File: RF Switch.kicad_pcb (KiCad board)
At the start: 2 copper layers, 60 x 52 mm, 16 parts

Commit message: Add files via upload
added decoupling capacitors C1 and C2, repositioned R1, R2 and R3
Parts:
- added C1: C_Small, Capacitor_THT:CP_Radial_D5.0mm_P2.00mm, F.Cu at (103.2, 119.9)
- added C2: C_Small, Capacitor_THT:C_Disc_D5.0mm_W2.5mm_P2.50mm, F.Cu at (117.7, 117.9)
- J4: renamed from  
- moved R1 17.8 mm to (114.0, 144.1), turned to 180 degrees
- moved R2 6.80 mm to (139.1, 135.9), turned to 180 degrees
- moved R3 5.48 mm to (135.3, 139.2), turned to 180 degrees
- renumbered LED to D1, Power to J1, Switch to J2, Selector to SW2, ATTiny84 to U1
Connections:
- R1 pad 1: Net-(J4-Pad2) -> Net-(D1-Pad1)
- R1 pad 2: Net-(D1-Pad4) -> Net-(R1-Pad2)
- R2 pad 1: Net-(J4-Pad4) -> Net-(D1-Pad4)
- R2 pad 2: Net-(D1-Pad3) -> Net-(J4-Pad6)
- R3 pad 1: Net-(J2-Pad2) -> Net-(D1-Pad3)
- R3 pad 2: Net-(D1-Pad1) -> Net-(J4-Pad4)
- U1 pad 6: Net-(U1-Pad6) -> Net-(R1-Pad2)
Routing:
- net Net-(J4-Pad6): track 30.3 -> 60.8 mm
- net Net-(D1-Pad1): track 25.5 -> 4.30 mm
- net Net-(J4-Pad2): track 53.9 -> 33.7 mm
- net Net-(D1-Pad4): track 3.78 -> 19.8 mm
- net Net-(J2-Pad2): track 27.7 -> 17.4 mm
- net Net-(J4-Pad4): track 57.3 -> 47.0 mm
- net Net-(R1-Pad2): track 0.00 -> 10.2 mm
- net Net-(D1-Pad3): track 12.9 -> 19.6 mm
- net Net-(C2-Pad1): track 34.2 -> 35.3 mm
- net Net-(J4-Pad5): track 22.8 -> 23.8 mm
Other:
- board text added: "Designed by Electrifying Rides electrifyingrides.com.au"
- board text added: "JLCJLCJLCJLC"
- board text added: "RF Transmitter Button HW Ver 1 .0 - FW Ver 1.0"

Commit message: Add files via upload
Added pull up resistor and C1/C2
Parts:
- added 10k: 10k, Resistor_THT:R_Axial_DIN0207_L6.3mm_D2.5mm_P10.16mm_Horizontal, F.Cu at (136.6, 132.8)
-  : renamed from J4; value Conn_01x06 -> Programming Connector
- 100nF: renamed from C1; value C_Small -> 100nf ceramic; footprint Capacitor_THT:CP_Radial_D5.0mm_P2.00mm -> Capacitor_THT:C_Disc_D5.0mm_W2.5mm_P2.50mm
- 10uF: renamed from C2; value C_Small -> 10uF electrolytic; footprint Capacitor_THT:C_Disc_D5.0mm_W2.5mm_P2.50mm -> Capacitor_THT:CP_Radial_D5.0mm_P2.00mm
- J6: renamed from  ; value Conn_01x01 -> On/Off Switch
- OFF: value Conn_01x01 -> NC On/Off switch
- ON: value Conn_01x01 -> On/Off Switch
- RF Module: value Conn_01x04 -> RF Module Header
- moved 10uF 0.50 mm to (117.7, 118.4)
- renumbered R3 to 220, R2 to 220, R1 to 220, U1 to ATTiny84, J1 to Power, SW2 to Selector, J2 to Switch
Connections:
-   pad 1: GND -> +VDC
-   pad 3: +VDC -> Net-(J4-Pad3)
-   pad 6: Net-(J4-Pad6) -> GND
- 220 pad 2: Net-(J4-Pad6) -> Net-(J4-Pad5)
- ATTiny84 pad 4: Net-(J4-Pad5) -> Net-(J4-Pad3)
- ATTiny84 pad 7: Net-(J4-Pad6) -> Net-(J4-Pad5)
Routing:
- net Net-(J4-Pad6): track 60.8 -> 0.00 mm
- net Net-(J4-Pad5): track 23.8 -> 70.9 mm
- net Net-(J4-Pad3): track 0.00 -> 37.0 mm, vias 0 -> 1
- net Net-(J2-Pad2): track 17.4 -> 29.7 mm
- net Net-(U1-Pad5): track 0.00 -> 5.07 mm, vias 0 -> 1

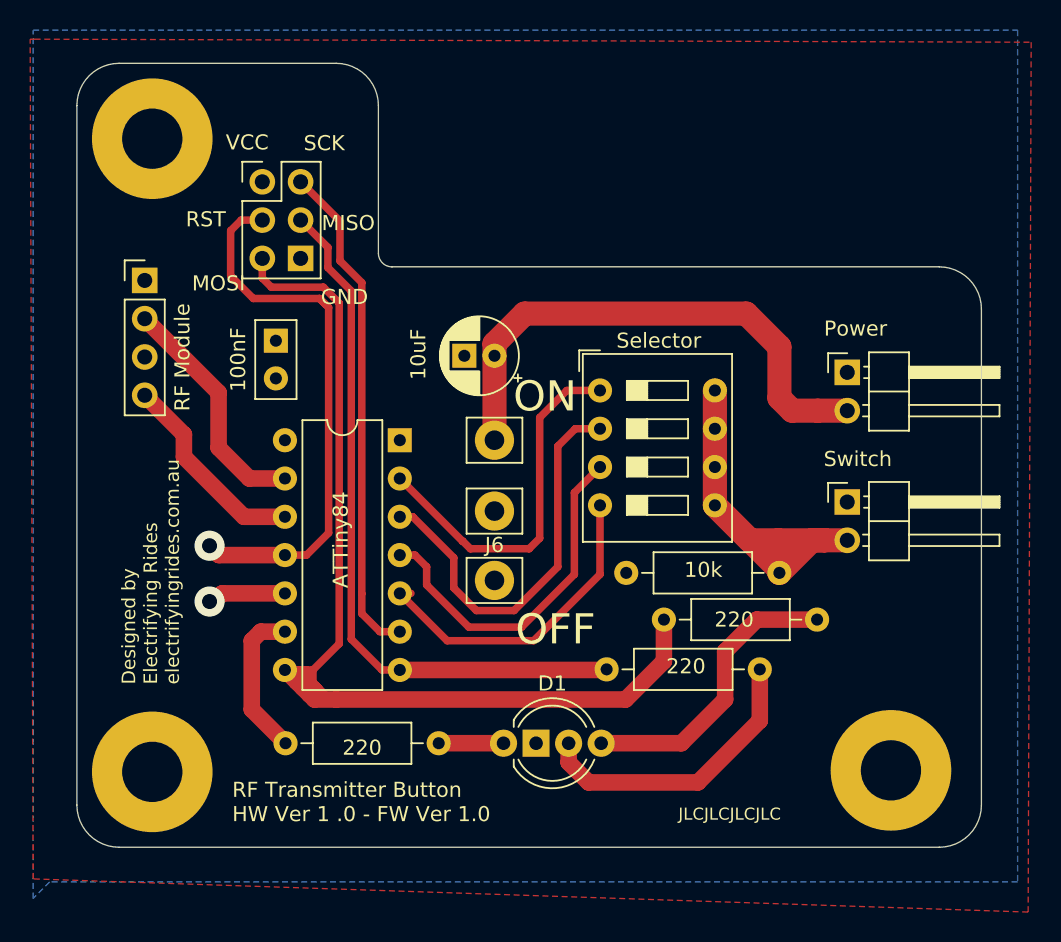
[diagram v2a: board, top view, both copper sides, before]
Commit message: Add files via upload
componet reposition
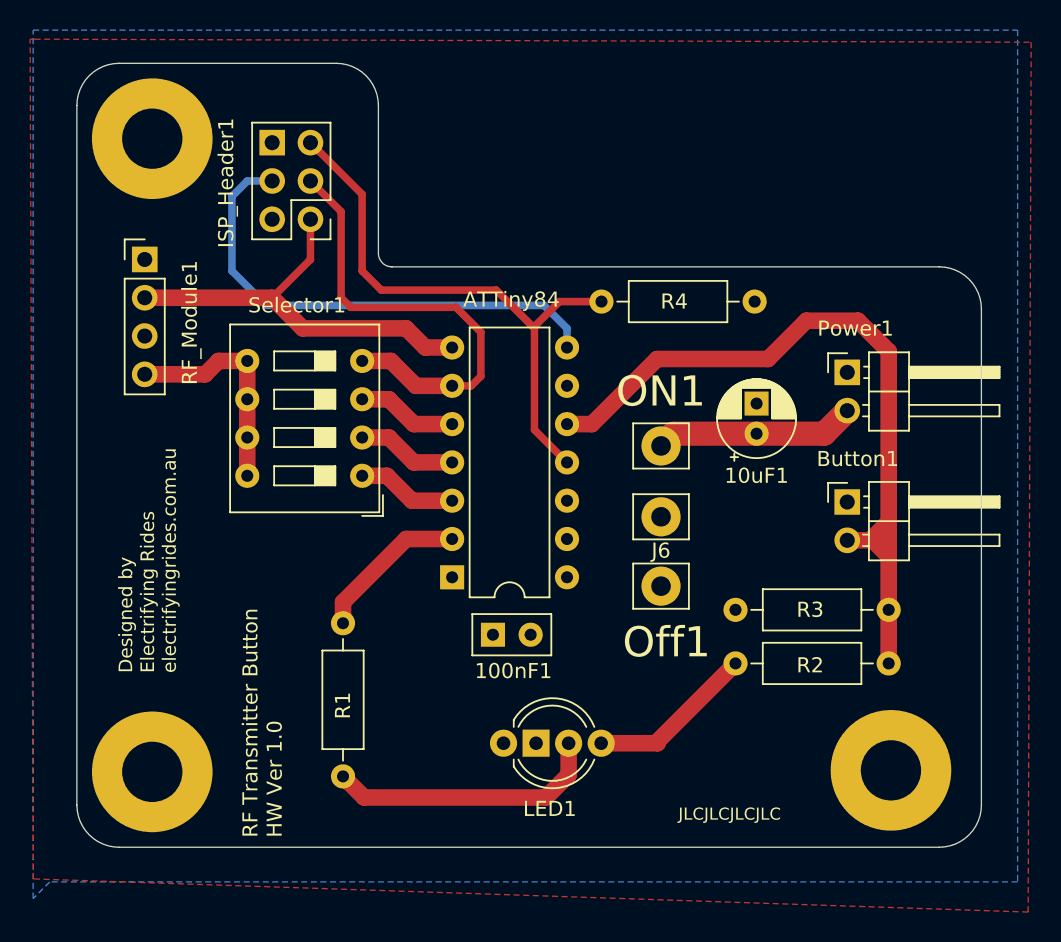
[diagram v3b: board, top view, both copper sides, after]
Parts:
- removed 220: R, Resistor_THT:R_Axial_DIN0207_L6.3mm_D2.5mm_P10.16mm_Horizontal
- added R4: 10k, Resistor_THT:R_Axial_DIN0207_L6.3mm_D2.5mm_P10.16mm_Horizontal, F.Cu at (124.8, 114.8)
- 100nF1: renamed from 100nF; value 100nf ceramic -> (none)
- 10uF1: renamed from 10uF; value 10uF electrolytic -> (none)
- Button1: renamed from Switch; value Button -> (none)
- ISP_Header1: renamed from  ; value Programming Connector -> (none)
- LED1: renamed from D1; value LED_BARG -> (none)
- ON1: renamed from ON; value On/Off Switch -> (none)
- Off1: renamed from OFF; value NC On/Off switch -> (none)
- Power1: renamed from Power; value Power -> (none)
- R1, R2: renamed from 220; value R -> R220
- RF_Module1: renamed from RF Module; value RF Module Header -> (none)
- Selector1: renamed from Selector; value Channel Selector -> (none)
- moved R1 28.5 mm to (107.7, 146.3), turned to 90 degrees
- moved 100nF1 24.0 mm to (120.1, 136.9), turned to 180 degrees
- moved ATTiny84 20.8 mm to (122.5, 133.1), turned to 180 degrees
- moved 10uF1 18.1 mm to (135.1, 123.6), turned to 90 degrees
- moved Selector1 16.8 mm to (108.9, 126.4), turned to 180 degrees
- moved J6 11.1 mm to (128.7, 129.1)
- moved ON1 11.1 mm to (128.7, 124.4)
- moved Off1 11.1 mm to (128.7, 133.7)
- moved R3 7.65 mm to (143.8, 135.3)
- moved R2 6.14 mm to (133.7, 138.8), turned to 0 degrees
- moved ISP_Header1 4.05 mm to (105.5, 109.3), turned to 180 degrees
- moved RF_Module1 1.39 mm to (94.5, 112.0)
- renumbered 10k to R3
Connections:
- ATTiny84 pad 10: Net-(SW2-Pad4) -> Net-(ATTiny84-Pad10)
- ATTiny84 pad 11: Net-(SW2-Pad3) -> Net-(ATTiny84-Pad11)
- ATTiny84 pad 12: Net-(SW2-Pad2) -> Net-(ATTiny84-Pad12)
- ATTiny84 pad 13: Net-(SW2-Pad1) -> Net-(ATTiny84-Pad13)
- ATTiny84 pad 2: Net-(RF1-Pad2) -> Net-(ATTiny84-Pad2)
- ATTiny84 pad 3: Net-(RF1-Pad4) -> Net-(ATTiny84-Pad3)
- ATTiny84 pad 4: Net-(J4-Pad3) -> Net-(ATTiny84-Pad4)
- ATTiny84 pad 5: Net-(U1-Pad5) -> Net-(ATTiny84-Pad5)
- ATTiny84 pad 7: Net-(J4-Pad5) -> Net-(ATTiny84-Pad7)
- ATTiny84 pad 8: Net-(J4-Pad4) -> Net-(ATTiny84-Pad8)
- ATTiny84 pad 9: Net-(J4-Pad2) -> Net-(ATTiny84-Pad9)
- Button1 pad 2: Net-(J2-Pad2) -> Net-(ATTiny84-Pad5)
- ISP_Header1 pad 1: +VDC -> Net-(ATTiny84-Pad8)
- ISP_Header1 pad 2: Net-(J4-Pad2) -> +VDC
- ISP_Header1 pad 3: Net-(J4-Pad3) -> Net-(ATTiny84-Pad9)
- ISP_Header1 pad 4: Net-(J4-Pad4) -> Net-(ATTiny84-Pad7)
- ISP_Header1 pad 5: Net-(J4-Pad5) -> Net-(ATTiny84-Pad4)
- R1 pad 2: Net-(J4-Pad4) -> Net-(ATTiny84-Pad13)
- R2 pad 2: Net-(J4-Pad5) -> Net-(ATTiny84-Pad5)
- R3 pad 1: Net-(J2-Pad2) -> Net-(ATTiny84-Pad5)
- RF_Module1 pad 2: Net-(RF1-Pad2) -> Net-(ATTiny84-Pad8)
- RF_Module1 pad 4: Net-(RF1-Pad4) -> Net-(RF_Module1-Pad4)
- Selector1 pad 1: Net-(SW2-Pad1) -> Net-(ATTiny84-Pad12)
- Selector1 pad 2: Net-(SW2-Pad2) -> Net-(ATTiny84-Pad11)
- Selector1 pad 3: Net-(SW2-Pad3) -> Net-(ATTiny84-Pad10)
- Selector1 pad 4: Net-(SW2-Pad4) -> Net-(ATTiny84-Pad9)
- Selector1 pad 5: Net-(J2-Pad2) -> Net-(RF_Module1-Pad4)
- Selector1 pad 6: Net-(J2-Pad2) -> Net-(RF_Module1-Pad4)
- Selector1 pad 7: Net-(J2-Pad2) -> Net-(RF_Module1-Pad4)
- Selector1 pad 8: Net-(J2-Pad2) -> Net-(RF_Module1-Pad4)
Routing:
- net Net-(J4-Pad5): track 70.9 -> 0.00 mm
- net Net-(ATTiny84-Pad5): track 0.00 -> 51.2 mm
- net Net-(J4-Pad4): track 47.0 -> 0.00 mm
- net Net-(ATTiny84-Pad4): track 0.00 -> 38.0 mm
- net Net-(J4-Pad3): track 37.0 -> 0.00 mm, vias 1 -> 0
- net Net-(J4-Pad2): track 33.3 -> 0.00 mm
- net Net-(ATTiny84-Pad7): track 0.00 -> 33.1 mm
- net Net-(ATTiny84-Pad9): track 0.00 -> 30.5 mm
- net Net-(J2-Pad2): track 29.7 -> 0.00 mm
- net Net-(ATTiny84-Pad8): track 0.00 -> 28.0 mm
- net Net-(SW2-Pad2): track 26.7 -> 0.00 mm
- net Net-(SW2-Pad1): track 24.2 -> 0.00 mm
- net Net-(SW2-Pad3): track 23.5 -> 0.00 mm
- net Net-(10uF1-Pad1): track 35.3 -> 13.3 mm
- net Net-(SW2-Pad4): track 21.7 -> 0.00 mm
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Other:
- board text added: "RF Transmitter Button HW Ver 1.0"
- board text removed: "GND"
- board text removed: "MISO"
- board text removed: "MOSI"
- board text removed: "RF Transmitter Button HW Ver 1 .0 - FW Ver 1.0"
- board text removed: "RST"
- board text removed: "SCK"
- board text removed: "VCC"
